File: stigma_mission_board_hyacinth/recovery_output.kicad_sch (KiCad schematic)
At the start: 20 parts, among them J17 Conn_02x02_Top_Bottom, Q10 DMN2056U, Q11 AOSP21321, U11 INA181

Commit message: fixed some errors
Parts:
- renumbered C29 to C48, C26 to C49, C27 to C50, C63 to C51, D13 to D20, D25 to D21, D14 to D22, F4 to F3, F5 to F4, J17 to J12, JP2 to JP7, JP6 to JP8, Q10 to Q4, Q11 to Q5, R20 to R45, R21 to R46, R18 to R47, R33 to R48, R22 to R49, U11 to U14

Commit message: placed recovery outputs and vehicle bus, fixed errors in schematic
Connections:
- net +3V3 is gone; now on net +3.3V: C49.2, C50.2
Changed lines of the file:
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@@
 			)
 		)
-		(property "Value" "+3V3"
+		(property "Value" "+3.3V"
 			(at 146.05 66.04 0)
 			(effects

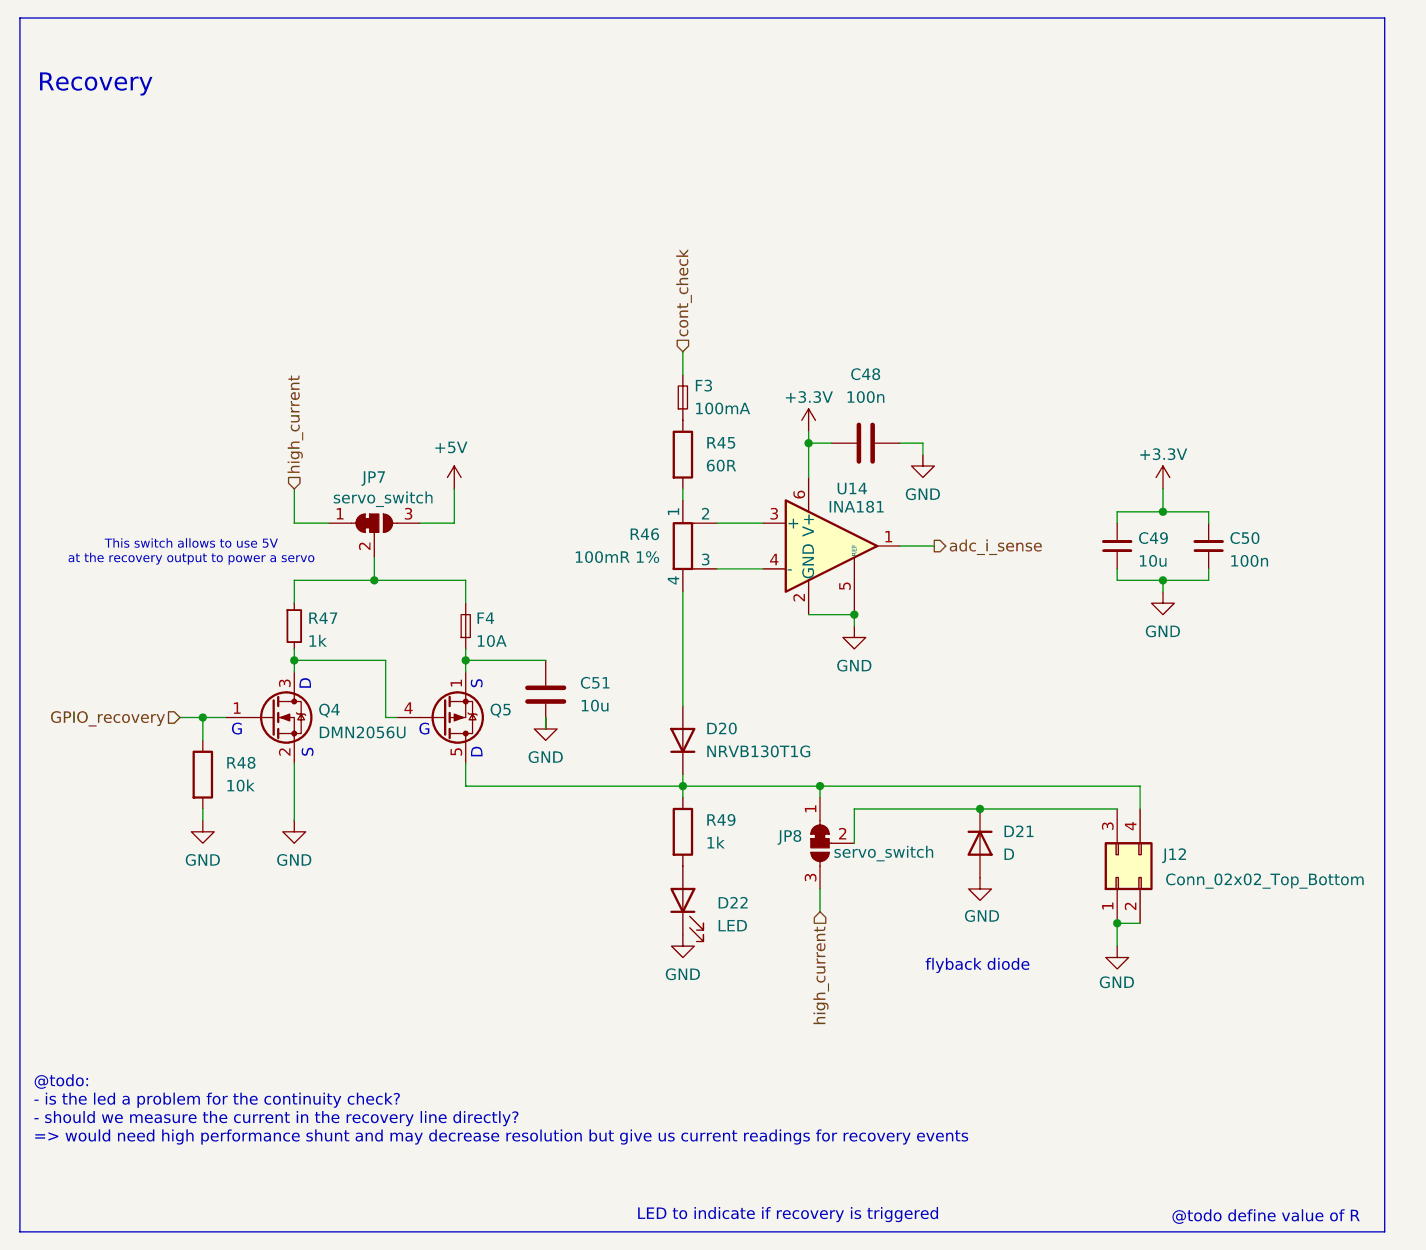
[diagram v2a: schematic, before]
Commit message: made board more compact, started routing recovery outputs
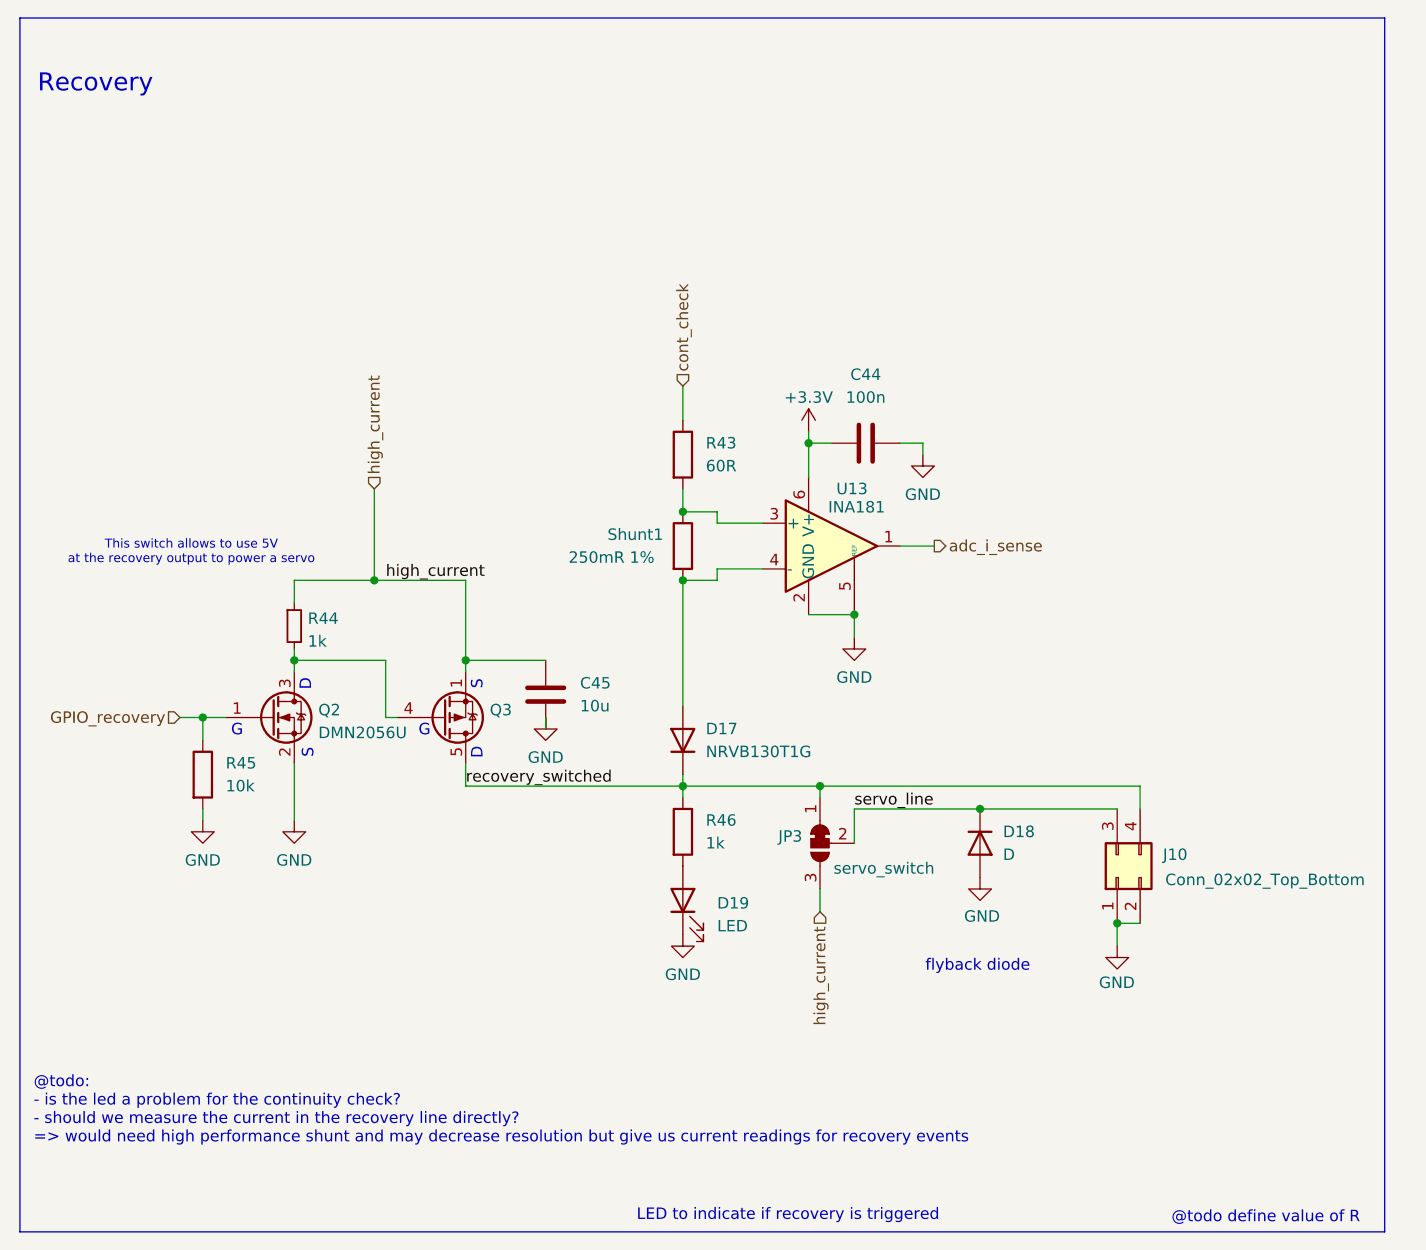
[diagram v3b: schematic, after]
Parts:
- removed C49: 10u, Capacitor_SMD:C_1206_3216Metric, symbol Device:C_Small
- removed C50: 100n, Capacitor_SMD:C_0603_1608Metric, symbol Device:C_Small
- removed F3: 100mA, Fuse:Fuse_1206_3216Metric, symbol Device:Fuse_Small
- removed F4: 10A, Fuse:Fuse_1206_3216Metric, symbol Device:Fuse_Small
- removed JP7: servo_switch, Jumper:SolderJumper-3_P1.3mm_Open_RoundedPad1.0x1.5mm, symbol Jumper:SolderJumper_3_Bridged12
- removed R46: 100mR 1%, Resistor_SMD:R_Shunt_Ohmite_LVK12, symbol Device:R_Shunt
- added Shunt1: 250mR 1%, Resistor_SMD:R_0805_2012Metric, symbol Device:R
- JP3: renamed from JP8; footprint Jumper:SolderJumper-3_P1.3mm_Open_RoundedPad1.0x1.5mm -> Jumper:SolderJumper-3_Open_RoundedPad2x2mm
- U13: renamed from U14; LCSC# (none) -> C2058842
- renumbered C48 to C44, C51 to C45, D20 to D17, D21 to D18, D22 to D19, J12 to J10, Q4 to Q2, Q5 to Q3, R45 to R43, R47 to R44, R48 to R45, R49 to R46
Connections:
- net cont_check: now also R43.1
- net high_current: now also C45.1, Q3.1 (S), Q3.2 (S), Q3.3 (S), R44.1
- net recovery_switched: now reaches D17.1 (K), J10.4 (Pin_4), JP3.1 (A), Q3.5 (D), Q3.6 (D), Q3.7 (D), Q3.8 (D), R46.1
- net servo_line: now reaches D18.1 (K), J10.3 (Pin_3), JP3.2 (C)
- net at R43.2: now also U13.3 (+), Shunt1.1
- net at U13.4 (-): now also D17.2 (A), Shunt1.2

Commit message: some tydiing up and adding footprints
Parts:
- JP3: footprint Jumper:SolderJumper-3_Open_RoundedPad2x2mm -> stigma:SolderJumper-3_Open_RoundedPad2x2mm
- renumbered R43 to R45, R44 to R46, R45 to R47, R46 to R48

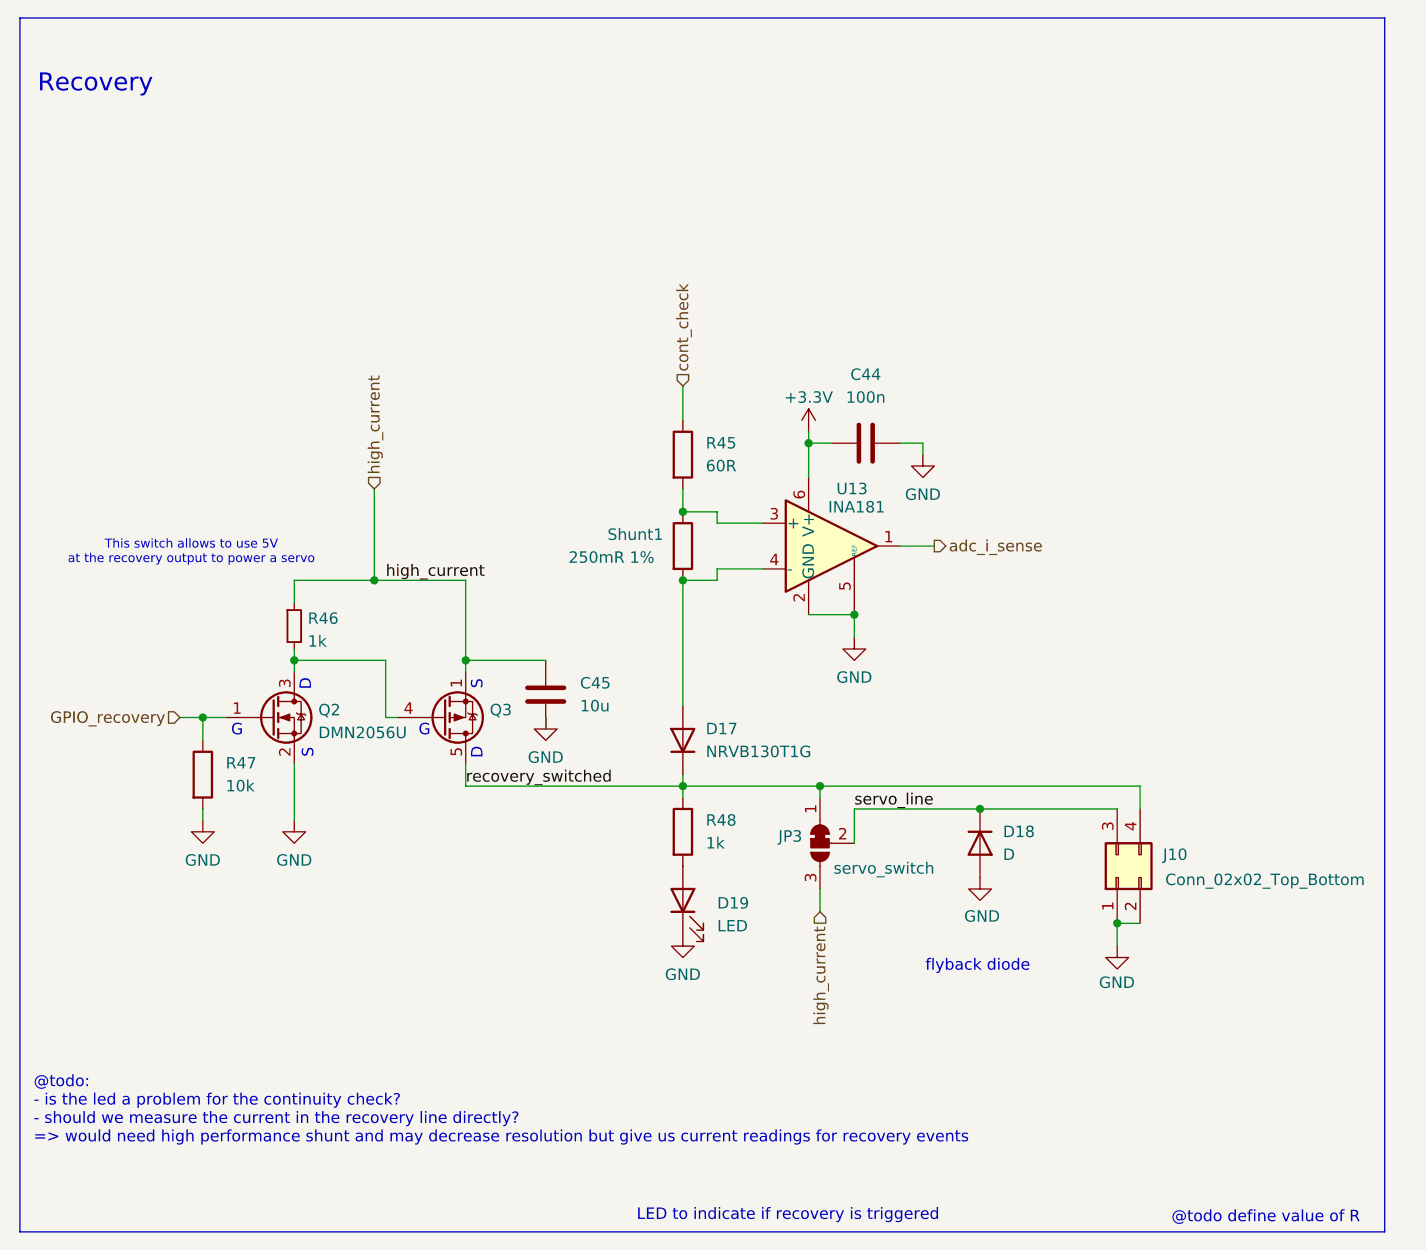
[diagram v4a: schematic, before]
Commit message: added the other 2 recovery outputs and sorted all components
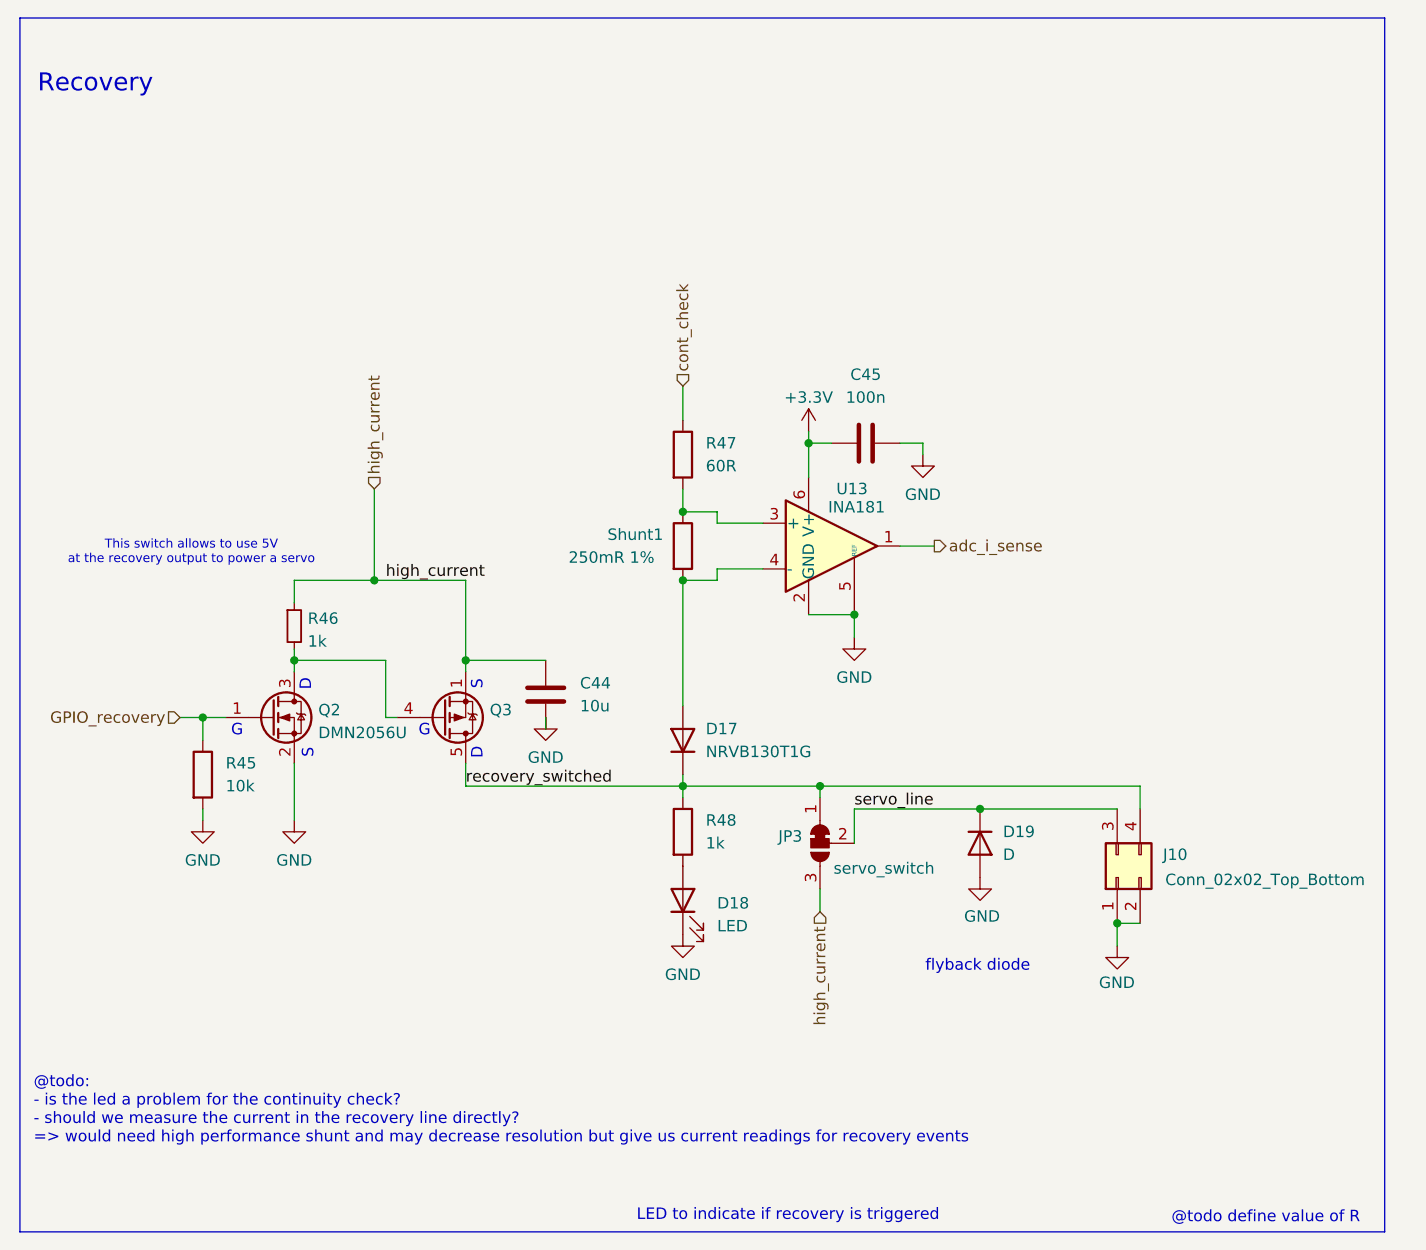
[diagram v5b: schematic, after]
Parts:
- JP3: footprint stigma:SolderJumper-3_Open_RoundedPad2x2mm -> Stigma:SolderJumper-3_Open_RoundedPad2x2mm
- renumbered C45 to C44, C44 to C45, D19 to D18, D18 to D19, R47 to R45, R45 to R47

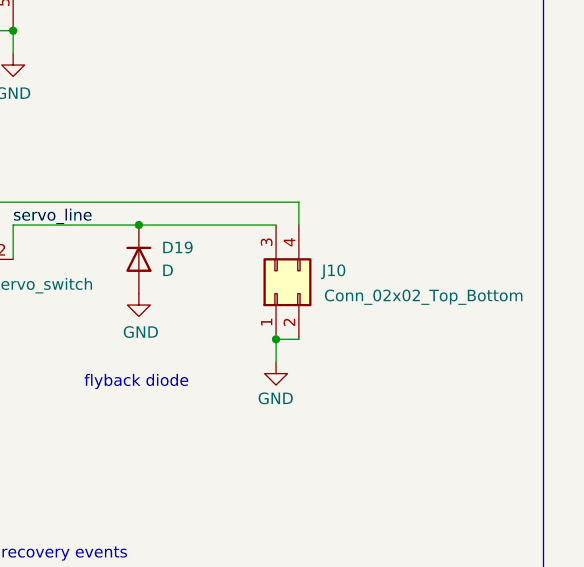
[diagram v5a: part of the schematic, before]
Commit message: added 3d models of connectors
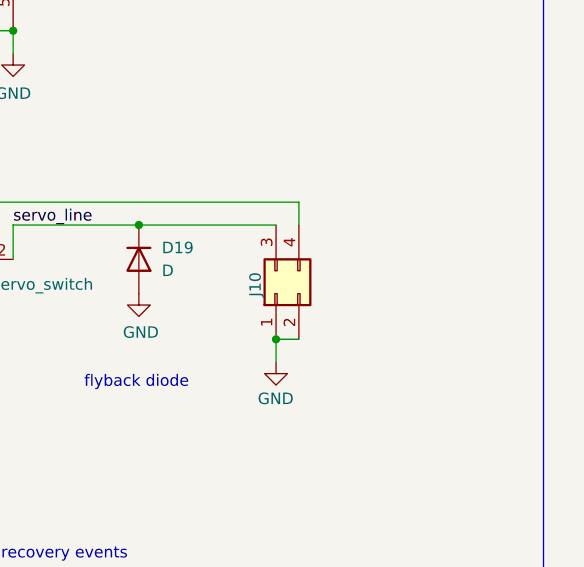
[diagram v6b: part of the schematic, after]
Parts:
- J10: value Conn_02x02_Top_Bottom -> (none)
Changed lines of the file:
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@@
-	)
-	(junction
-		(at 140.97 118.11)
-		(diameter 0)
-		(color 0 0 0 0)
 	)
 	(junction
@@
 	(junction
 		(at 106.68 64.77)
+		(diameter 0)
+		(color 0 0 0 0)
+	)
+	(junction
+		(at 140.97 118.11)
 		(diameter 0)
 		(color 0 0 0 0)
@@
 				(path "/34e067c7-b84e-477a-88f3-7322f422dd23/9351aa18-d08f-4bdd-8577-c307d483b4c3"
 					(reference "JP5")
+					(unit 1)
+				)
+			)
+		)
+	)
+	(symbol
+		(lib_id "Connector_Generic:Conn_02x02_Top_Bottom")
+		(at 140.97 113.03 90)
+		(unit 1)
+		(exclude_from_sim no)
+		(in_bom yes)
+		(on_board yes)
+		(dnp no)
+		(property "Reference" "J10"
+			(at 138.684 112.014 0)
+			(effects
+				(font
+					(size 1.27 1.27)
+				)
+			)
+		)
+		(property "Value" ""
+			(at 137.414 113.284 0)
+			(effects
+				(font
+					(size 1.27 1.27)
+				)
+				(hide yes)
+			)
+		)
+		(property "Footprint" "Connector_Molex:Molex_Micro-Fit_3.0_43045-0400_2x02_P3.00mm_Horizontal"
+			(at 140.97 113.03 0)
+			(effects
+				(font
+					(size 1.27 1.27)
+				)
+				(hide yes)
+			)
+		)
+		(property "Datasheet" ""
+			(at 140.97 113.03 0)
+			(effects
+				(font
+					(size 1.27 1.27)
+				)
+				(hide yes)
+			)
+		)
+		(property "Description" ""
+			(at 140.97 113.03 0)
+			(effects
+				(font
+					(size 1.27 1.27)
+				)
+				(hide yes)
+			)
+		)
+		(pin "3"
+		)
+		(pin "2"
+		)
+		(pin "4"
+		)
+		(pin "1"
+		)
+		(instances
+			(project "stigma_mission_board_hysteresis"
+				(path "/34e067c7-b84e-477a-88f3-7322f422dd23/1b0ab639-d420-4016-938c-453dcf1ed81d"
+					(reference "J11")
+					(unit 1)
+				)
+				(path "/34e067c7-b84e-477a-88f3-7322f422dd23/1e21a0b4-3701-4fea-ae6f-c1650f6b51b3"
+					(reference "J10")
+					(unit 1)
+				)
+				(path "/34e067c7-b84e-477a-88f3-7322f422dd23/4924f453-debe-420b-955f-34707f20b488"
+					(reference "J13")
+					(unit 1)
+				)
+				(path "/34e067c7-b84e-477a-88f3-7322f422dd23/9351aa18-d08f-4bdd-8577-c307d483b4c3"
+					(reference "J12")
 					(unit 1)
 				)
@@
 					(unit 1)
 				)
-			)
-		)
-	)
-	(symbol
-		(lib_id "Connector_Generic:Conn_02x02_Top_Bottom")
-		(at 140.97 113.03 90)
-		(unit 1)
-		(exclude_from_sim no)
-		(in_bom yes)
-		(on_board yes)
-		(dnp no)
-		(property "Reference" "J10"
-			(at 146.05 110.4899 90)
-			(effects
-				(font
-					(size 1.27 1.27)
-				)
-				(justify right)
-			)
-		)
-		(property "Value" "Conn_02x02_Top_Bottom"
-			(at 146.304 113.284 90)
-			(effects
-				(font
-					(size 1.27 1.27)
-				)
-				(justify right)
-			)
-		)
-		(property "Footprint" "Connector_Molex:Molex_Micro-Fit_3.0_43045-0400_2x02_P3.00mm_Horizontal"
-			(at 140.97 113.03 0)
-			(effects
-				(font
-					(size 1.27 1.27)
-				)
-				(hide yes)
-			)
-		)
-		(property "Datasheet" "~"
-			(at 140.97 113.03 0)
-			(effects
-				(font
-					(size 1.27 1.27)
-				)
-				(hide yes)
-			)
-		)
-		(property "Description" "Generic connector, double row, 02x02, top/bottom pin numbering scheme (row 1: 1...pins_per_row, row2: pins_per_row+1 ... num_pins), script generated (kicad-library-utils/schlib/autogen/connector/)"
-			(at 140.97 113.03 0)
-			(effects
-				(font
-					(size 1.27 1.27)
-				)
-				(hide yes)
-			)
-		)
-		(pin "4"
-		)
-		(pin "1"
-		)
-		(pin "3"
-		)
-		(pin "2"
-		)
-		(instances
-			(project "stigma_mission_board_hysteresis"
-				(path "/34e067c7-b84e-477a-88f3-7322f422dd23/1b0ab639-d420-4016-938c-453dcf1ed81d"
-					(reference "J11")
-					(unit 1)
-				)
-				(path "/34e067c7-b84e-477a-88f3-7322f422dd23/1e21a0b4-3701-4fea-ae6f-c1650f6b51b3"
-					(reference "J10")
-					(unit 1)
-				)
-				(path "/34e067c7-b84e-477a-88f3-7322f422dd23/4924f453-debe-420b-955f-34707f20b488"
-					(reference "J13")
-					(unit 1)
-				)
-				(path "/34e067c7-b84e-477a-88f3-7322f422dd23/9351aa18-d08f-4bdd-8577-c307d483b4c3"
-					(reference "J12")
-					(unit 1)
-				)

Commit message: changed pcb design. currently not working
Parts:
- J10: value (none) -> ~
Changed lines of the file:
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@@
 			)
 		)
-		(property "Value" ""
+		(property "Value" "~"
 			(at 137.414 113.284 0)
 			(effects
